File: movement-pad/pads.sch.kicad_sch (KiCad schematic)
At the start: 11 parts, among them U1 74LS147

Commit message: updated fsr
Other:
- moved on the sheet: FSR1

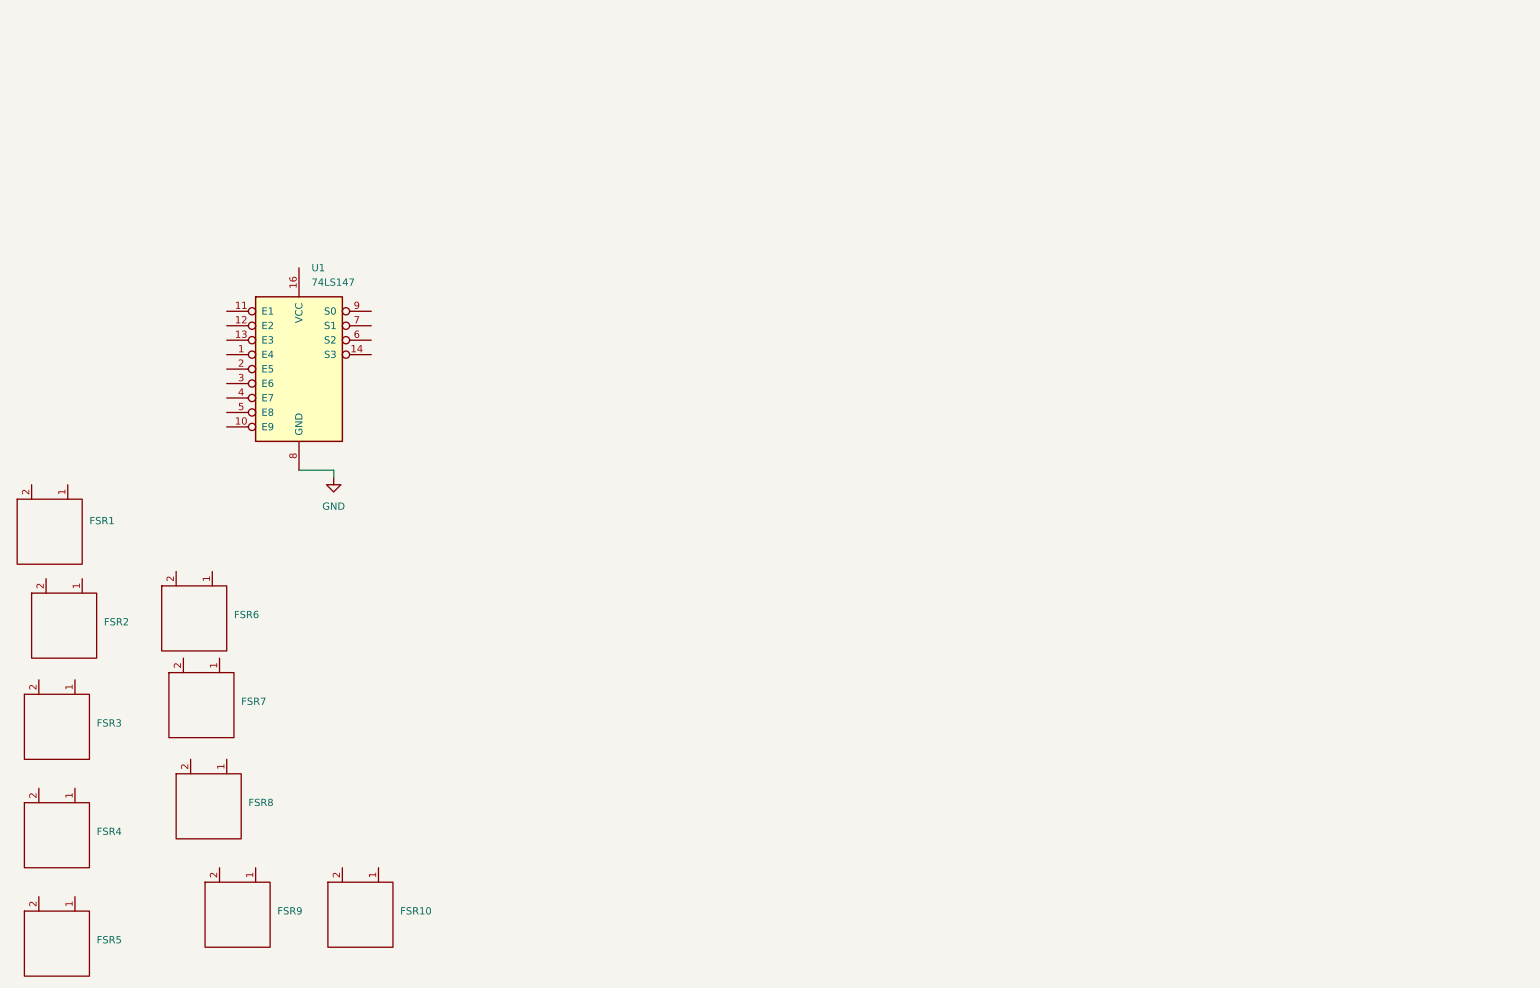
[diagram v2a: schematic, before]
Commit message: updated movement pad
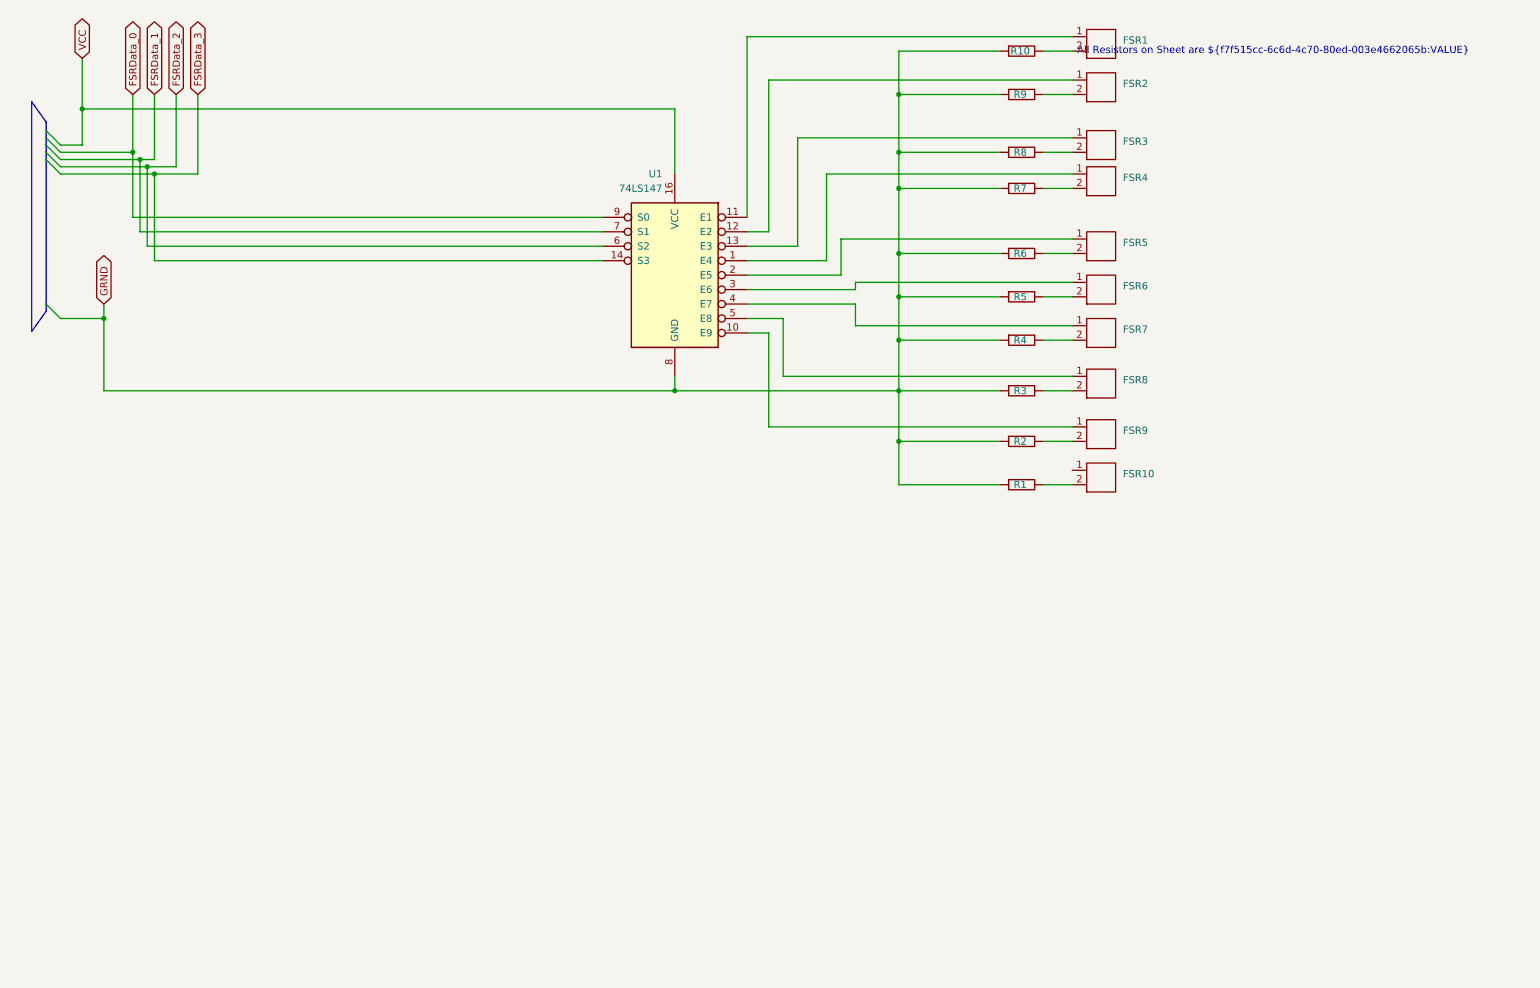
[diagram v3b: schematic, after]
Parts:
- added R1, R10, R2, R3, R4, R5, R6, R7, R8, R9: 390ohm, Resistor_THT:R_Axial_DIN0207_L6.3mm_D2.5mm_P10.16mm_Horizontal, symbol PCM_SL_Resistors:390ohm
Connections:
- net at FSR8.1: now also U1.5 (E8)
- net at FSR8.2: now also R3.2
- net at U1.1 (E4): now also FSR4.1
- net at U1.10 (E9): now also FSR9.1
- net at U1.11 (E1): now also FSR1.1
- net at U1.12 (E2): now also FSR2.1
- net at U1.13 (E3): now also FSR3.1
- net FSRData_3: now reaches U1.14 (S3)
- net VCC: now reaches U1.16 (VCC)
- net at U1.2 (E5): now also FSR5.1
- net at U1.3 (E6): now also FSR6.1
- net at U1.4 (E7): now also FSR7.1
- net FSRData_2: now reaches U1.6 (S2)
- net FSRData_1: now reaches U1.7 (S1)
- net FSRData_0: now reaches U1.9 (S0)
- net at FSR3.2: now also R8.2
- net at FSR2.2: now also R9.2
- net at FSR5.2: now also R6.2
- net at FSR4.2: now also R7.2
- net at FSR9.2: now also R2.2
- net at FSR6.2: now also R5.2
- net at FSR10.2: now also R1.2
- net at FSR1.2: now also R10.2
- net at FSR7.2: now also R4.2
- net GND renamed GRND
- net GRND: now also R1.1, R10.1, R2.1, R3.1, R4.1, R5.1, R6.1, R7.1, R8.1, R9.1
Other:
- note added: "All Resistors on Sheet are ${f7f515cc-6c6d-4c70-80ed-003e4662065b:VALUE}"
- moved on the sheet: U1
